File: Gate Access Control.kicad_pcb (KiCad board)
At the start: 2 copper layers, 20 parts, among them J1 Screw_Terminal_01x02, J2 RF Receiver 433MHz, J3 Conn_01x08, J4 IR_SENSORT, J5 Screw_Terminal_01x04, J6 Screw_Terminal_01x02, J7 Screw_Terminal_01x02, J8 Conn_01x06, U1 ATmega328-MM, Y1 Crystal

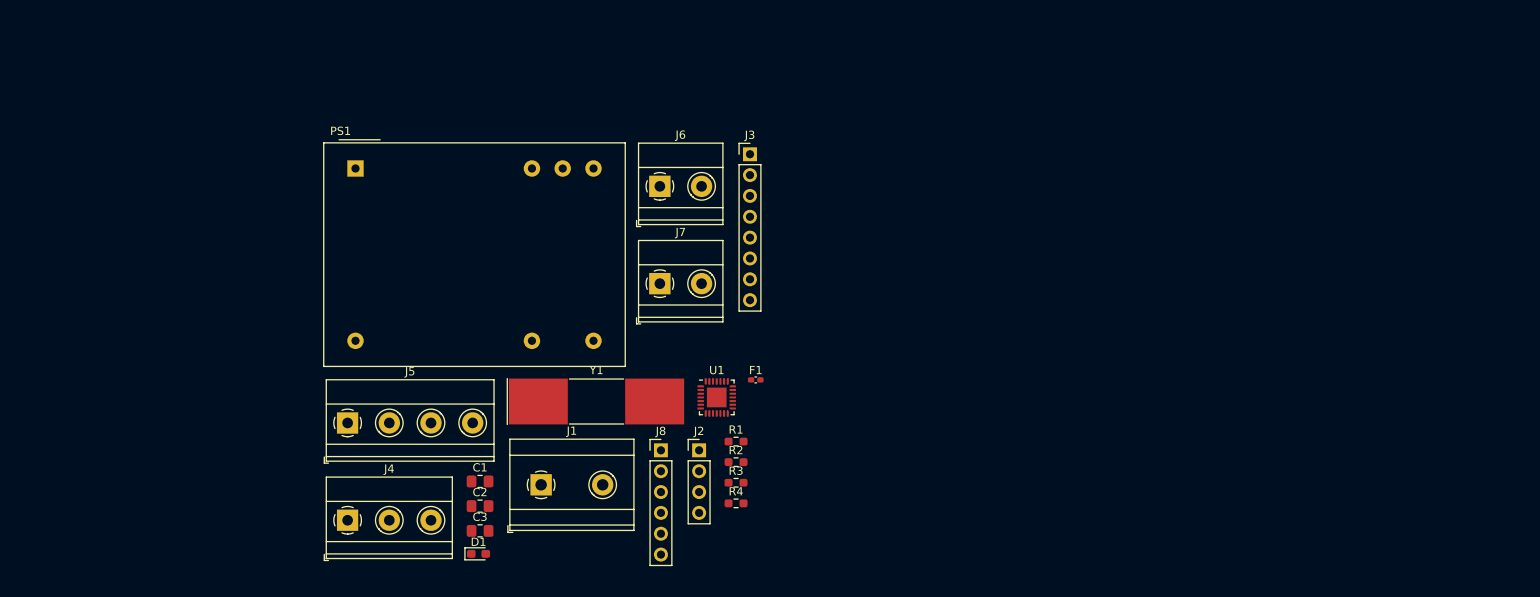
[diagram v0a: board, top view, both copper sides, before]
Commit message: Segregated & Placed Component Blocks
Also added one more size of track width to Predefined Sizes for the AC power.
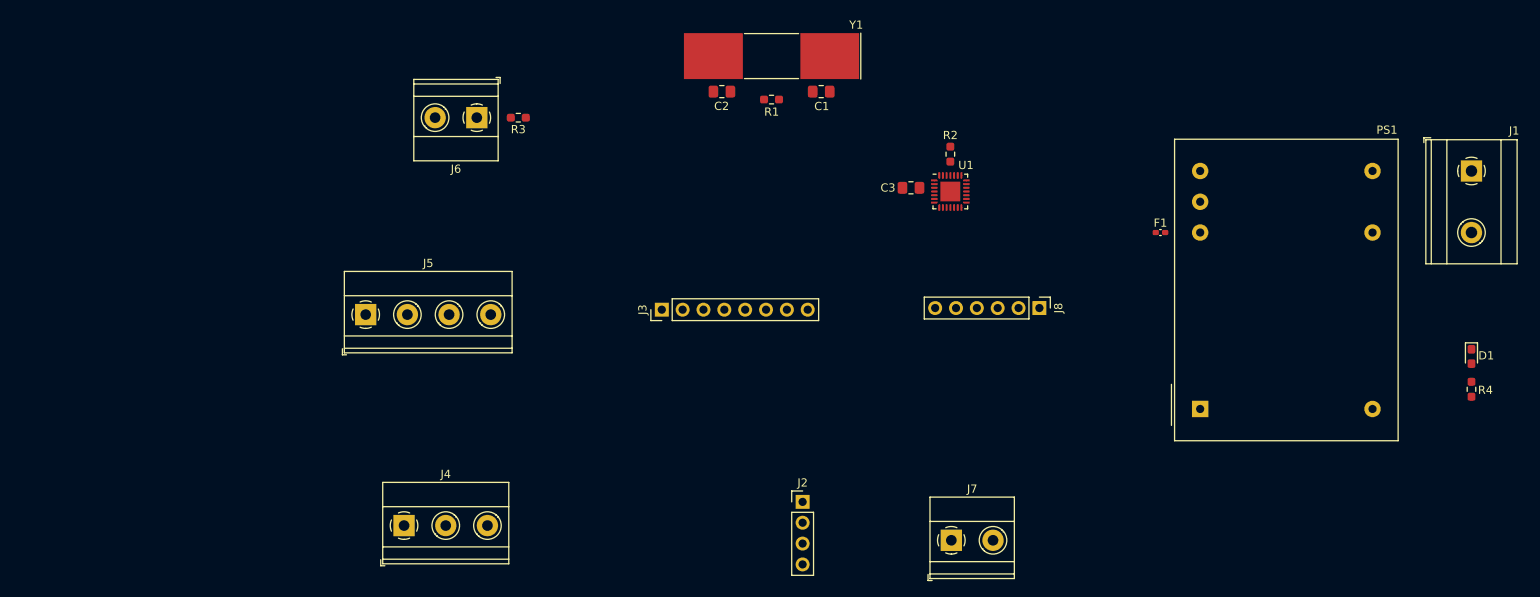
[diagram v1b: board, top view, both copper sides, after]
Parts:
- moved D1 123.4 mm to (229.7, 86.1), turned to -90 degrees
- moved J1 119.6 mm to (229.7, 63.5), turned to -90 degrees
- moved PS1 107.0 mm to (196.6, 92.5), turned to 90 degrees
- moved R4 90.7 mm to (229.7, 90.1), turned to -90 degrees
- moved C3 67.1 mm to (161.4, 65.5)
- moved C1 63.1 mm to (150.5, 53.8)
- moved C2 58.5 mm to (138.4, 53.8), turned to 180 degrees
- moved F1 52.5 mm to (191.8, 71.0)
- moved R3 51.8 mm to (113.6, 57.0), turned to 180 degrees
- moved J8 49.3 mm to (177.1, 80.2), turned to -90 degrees
- moved J7 47.3 mm to (166.3, 108.5)
- moved Y1 47.2 mm to (144.4, 49.5), turned to 180 degrees
- moved R2 45.7 mm to (166.2, 61.5), turned to 90 degrees
- moved R1 41.9 mm to (144.4, 54.8)
- moved U1 37.9 mm to (166.2, 66.0)
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
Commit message: Arranged Component Blocks in PCB
Changed the orders of pins on some connectors.
Design #1
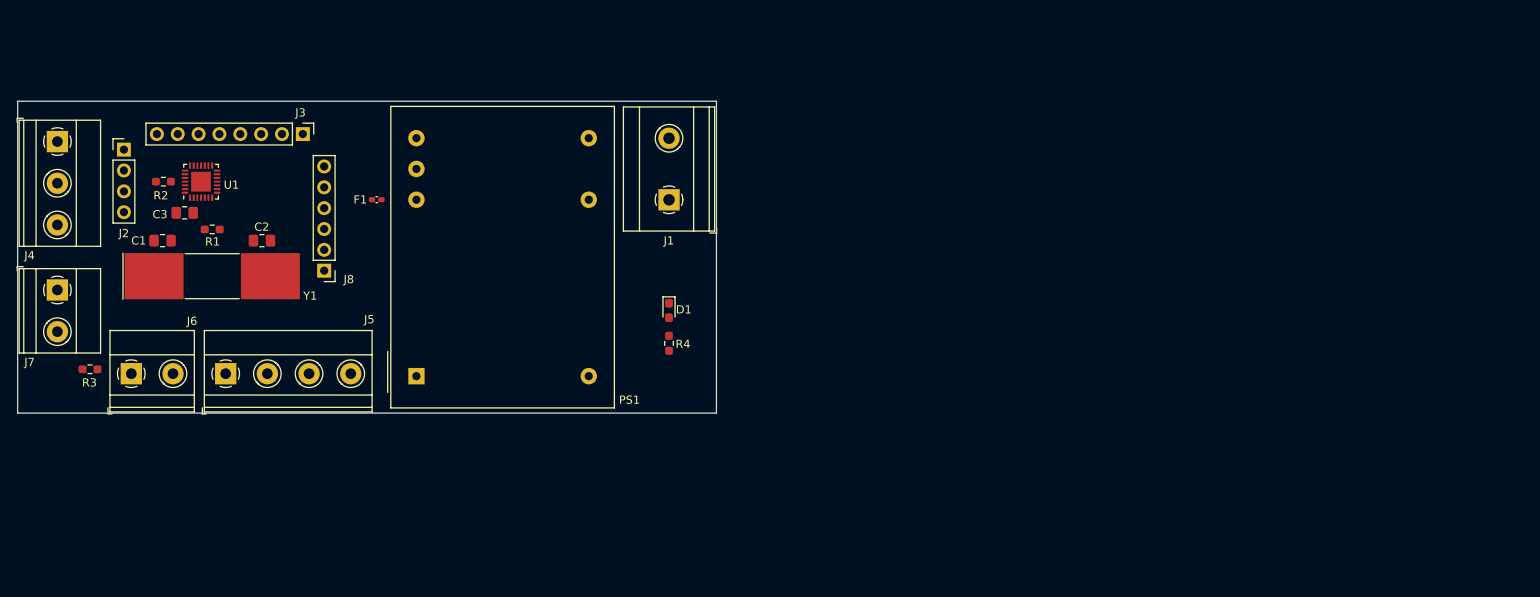
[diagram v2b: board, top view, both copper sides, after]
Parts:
- moved J7 113.1 mm to (57.4, 78.0), turned to -90 degrees
- moved D1 97.9 mm to (131.9, 80.5)
- moved R4 97.9 mm to (131.9, 84.5)
- moved J1 97.8 mm to (131.9, 67.0), turned to 90 degrees
- moved R2 95.9 mm to (70.3, 64.8), turned to 180 degrees
- moved F1 95.6 mm to (96.3, 67.0)
- moved PS1 95.6 mm to (101.1, 88.5)
- moved J2 93.2 mm to (65.5, 60.9)
- moved U1 91.3 mm to (74.9, 64.8), turned to 90 degrees
- moved C3 88.6 mm to (72.9, 68.6)
- moved J8 87.3 mm to (89.9, 75.7), turned to 180 degrees
- moved C1 82.3 mm to (70.2, 72.0), turned to 180 degrees
- moved Y1 73.2 mm to (76.3, 76.3), turned to 0 degrees
- moved R1 70.0 mm to (76.3, 70.6), turned to 180 degrees
- moved J4 63.0 mm to (57.4, 59.9), turned to -90 degrees
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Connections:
- J3 pad 1: /SDA/SS -> /RST
- J3 pad 2: /SCK -> /SDA/SS
- J3 pad 5: /IRQ -> /SCK
- J3 pad 7: /RST -> /IRQ
- J4 pad 2: GND -> +5V
- J4 pad 3: +5V -> GND
- J5 pad 1: /Enable -> /Inverter PWM
- J5 pad 2: /Inverter PWM -> /Enable
- J8 pad 2: /SCK -> /RESET
- J8 pad 5: /RESET -> /SCK
- PS1 pad 5: Net-(J1-Pin_1) -> Net-(J1-Pin_2)
- PS1 pad 6: Net-(J1-Pin_2) -> Net-(J1-Pin_1)
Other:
- board outline added: 85.1 x 38 mm
